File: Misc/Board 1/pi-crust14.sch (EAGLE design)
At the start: 43 parts, among them IC10 40193N, IC2 74LS595D, IC3 74LS595D, IC4 74LS595D, IC5 74LS595D, IC6 74LS595D, IC7 74LS595D, IC8 74AC11008, U1 AD9983AKSTZ_140, U2 SN54LS253_J_16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

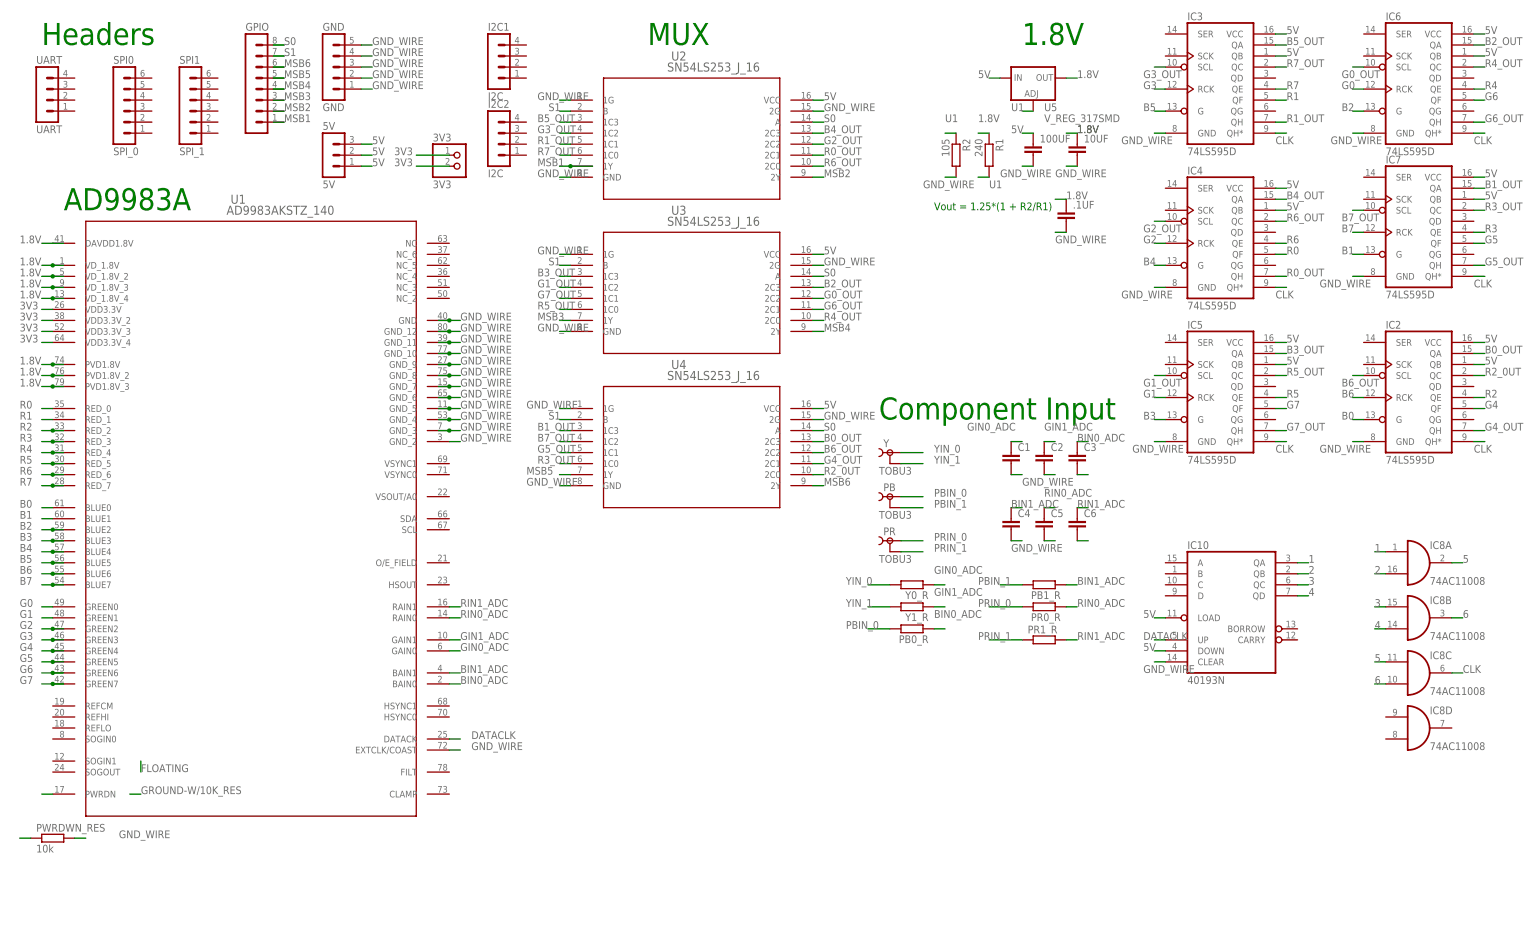
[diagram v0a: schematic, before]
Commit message: Board Update 4
Email sent to CUI for RCA Eagle File, RPI 2 female pins added to board,
ADC pins configured
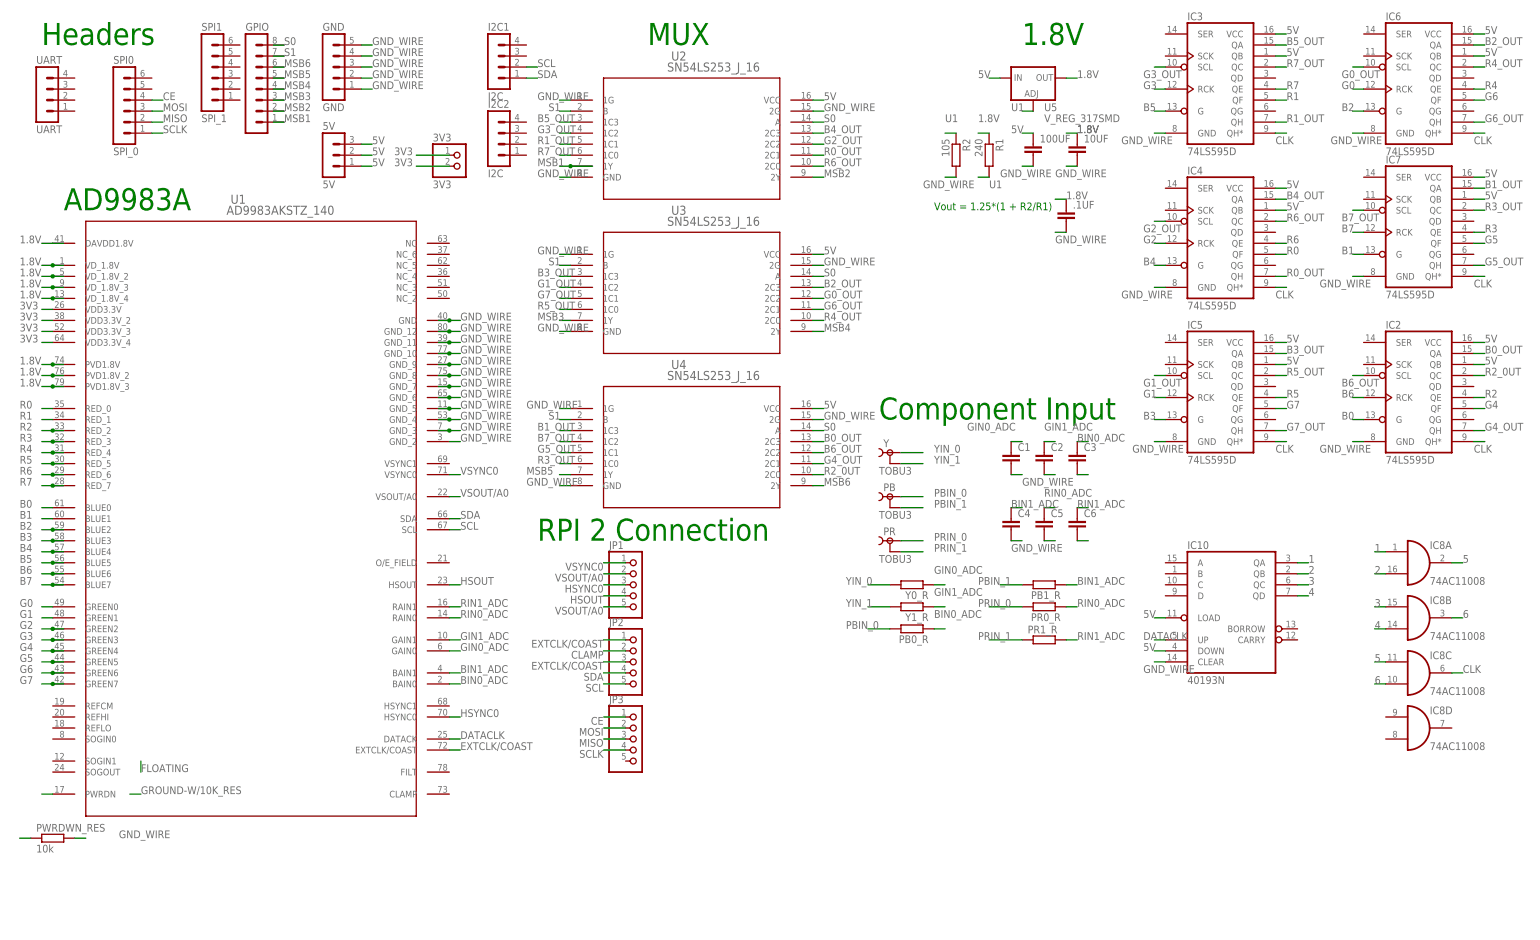
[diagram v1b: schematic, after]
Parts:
- added JP1, JP2, JP3: (no value), pinhead:PINHD-1X5
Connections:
- new net CE: JP3.1, SPI0.4
- new net CLAMP: JP2.2
- new net EXTCLK/COAST: JP2.1, JP2.3, U1.EXTCLK/COAST
- new net HSOUT: JP1.4, U1.HSOUT
- new net HSYNC0: JP1.3, U1.HSYNC0
- new net MISO: JP3.3, SPI0.2
- new net MOSI: JP3.2, SPI0.3
- new net SCL: I2C1.2, JP2.5, U1.SCL
- new net SCLK: JP3.4, SPI0.1
- new net SDA: I2C1.1, JP2.4, U1.SDA
- new net VSOUT/A0: JP1.2, JP1.5, U1.VSOUT/A0
- new net VSYNC0: JP1.1, U1.VSYNC0
- net GND_WIRE: no longer U1.EXTCLK/COAST
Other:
- note added: "RPI 2 Connection"
- moved on the sheet: SPI1
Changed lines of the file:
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@@
 <part name=".1UF" library="capacitor-wima" deviceset="C" device="2.5/5"/>
 <part name="U5" library="SparkFun-PowerIC" deviceset="V_REG_317" device="SMD"/>
+<part name="JP1" library="pinhead" deviceset="PINHD-1X5" device=""/>
+<part name="JP2" library="pinhead" deviceset="PINHD-1X5" device=""/>
+<part name="JP3" library="pinhead" deviceset="PINHD-1X5" device=""/>
 </parts>
 <sheets>
@@
 <text x="231.14" y="177.8" size="5.08" layer="91">1.8V</text>
 <text x="210.82" y="139.7" size="1.778" layer="91">Vout = 1.25*(1 + R2/R1)</text>
+<text x="119.38" y="63.5" size="5.08" layer="91">RPI 2 Connection</text>
 </plain>
 <instances>
@@
 <instance part="GND" gate="G$1" x="71.12" y="172.72"/>
 <instance part="SPI0" gate="1" x="22.86" y="165.1"/>
-<instance part="SPI1" gate="1" x="38.1" y="165.1"/>
+<instance part="SPI1" gate="1" x="43.18" y="172.72"/>
 <instance part="GPIO" gate="1" x="53.34" y="167.64"/>
 <instance part="3V3" gate="G$1" x="101.6" y="149.86"/>
@@
 <instance part=".1UF" gate="G$1" x="241.3" y="139.7"/>
 <instance part="U5" gate="G$1" x="233.68" y="170.18"/>
+<instance part="JP1" gate="A" x="142.24" y="53.34"/>
+<instance part="JP2" gate="A" x="142.24" y="35.56"/>
+<instance part="JP3" gate="A" x="142.24" y="17.78"/>
 </instances>
 <busses>
@@
 </segment>
 <segment>
-<wire x1="99.06" y1="15.24" x2="101.6" y2="15.24" width="0.3048" layer="91"/>
-<label x="104.14" y="15.24" size="1.778" layer="95"/>
-<pinref part="U1" gate="A" pin="EXTCLK/COAST"/>
-</segment>
-<segment>
 <wire x1="233.68" y1="149.86" x2="231.14" y2="149.86" width="0.8128" layer="91"/>
 <label x="226.06" y="147.32" size="1.778" layer="95"/>
@@
 <pinref part="U1" gate="A" pin="DATACK"/>
 <wire x1="99.06" y1="17.78" x2="101.6" y2="17.78" width="0.3048" layer="91"/>
-<label x="104.14" y="17.78" size="1.778" layer="95"/>
+<label x="101.6" y="17.78" size="1.778" layer="95"/>
 </segment>
 <segment>
@@
 </segment>
 </net>
+<net name="SDA" class="0">
+<segment>
+<pinref part="I2C1" gate="1" pin="1"/>
+<wire x1="116.84" y1="170.18" x2="119.38" y2="170.18" width="0.3048" layer="91"/>
+<label x="119.38" y="170.18" size="1.778" layer="95"/>
+</segment>
+<segment>
+<wire x1="134.62" y1="33.02" x2="139.7" y2="33.02" width="0.3048" layer="91"/>
+<label x="134.62" y="33.02" size="1.778" layer="95" rot="R180"/>
+<pinref part="JP2" gate="A" pin="4"/>
+</segment>
+<segment>
+<wire x1="99.06" y1="68.58" x2="101.6" y2="68.58" width="0.3048" layer="91"/>
+<label x="101.6" y="68.58" size="1.778" layer="95"/>
+<pinref part="U1" gate="A" pin="SDA"/>
+</segment>
+</net>
+<net name="SCL" class="0">
+<segment>
+<pinref part="I2C1" gate="1" pin="2"/>
+<wire x1="116.84" y1="172.72" x2="119.38" y2="172.72" width="0.3048" layer="91"/>
+<label x="119.38" y="172.72" size="1.778" layer="95"/>
+</segment>
+<segment>
+<wire x1="134.62" y1="30.48" x2="139.7" y2="30.48" width="0.3048" layer="91"/>
+<label x="134.62" y="30.48" size="1.778" layer="95" rot="R180"/>
+<pinref part="JP2" gate="A" pin="5"/>
+</segment>
+<segment>
+<wire x1="99.06" y1="66.04" x2="101.6" y2="66.04" width="0.3048" layer="91"/>
+<label x="101.6" y="66.04" size="1.778" layer="95"/>
+<pinref part="U1" gate="A" pin="SCL"/>
+</segment>
+</net>
+<net name="SCLK" class="0">
+<segment>
+<pinref part="SPI0" gate="1" pin="1"/>
+<wire x1="30.48" y1="157.48" x2="33.02" y2="157.48" width="0.3048" layer="91"/>
+<label x="33.02" y="157.48" size="1.778" layer="95"/>
+</segment>
+<segment>
+<wire x1="134.62" y1="15.24" x2="139.7" y2="15.24" width="0.3048" layer="91"/>
+<label x="134.62" y="15.24" size="1.778" layer="95" rot="R180"/>
+<pinref part="JP3" gate="A" pin="4"/>
+</segment>
+</net>
+<net name="MISO" class="0">
+<segment>
+<pinref part="SPI0" gate="1" pin="2"/>
+<wire x1="30.48" y1="160.02" x2="33.02" y2="160.02" width="0.3048" layer="91"/>
+<label x="33.02" y="160.02" size="1.778" layer="95"/>
+</segment>
+<segment>
+<wire x1="134.62" y1="17.78" x2="139.7" y2="17.78" width="0.3048" layer="91"/>
+<label x="134.62" y="17.78" size="1.778" layer="95" rot="R180"/>
+<pinref part="JP3" gate="A" pin="3"/>
+</segment>
+</net>
+<net name="MOSI" class="0">
+<segment>
+<pinref part="SPI0" gate="1" pin="3"/>
+<wire x1="30.48" y1="162.56" x2="33.02" y2="162.56" width="0.3048" layer="91"/>
+<label x="33.02" y="162.56" size="1.778" layer="95"/>
+</segment>
+<segment>
+<wire x1="134.62" y1="20.32" x2="139.7" y2="20.32" width="0.3048" layer="91"/>
+<label x="134.62" y="20.32" size="1.778" layer="95" rot="R180"/>
+<pinref part="JP3" gate="A" pin="2"/>
+</segment>
+</net>
+<net name="CE" class="0">
+<segment>
+<pinref part="SPI0" gate="1" pin="4"/>
+<wire x1="30.48" y1="165.1" x2="33.02" y2="165.1" width="0.3048" layer="91"/>
+<label x="33.02" y="165.1" size="1.778" layer="95"/>
+</segment>
+<segment>
+<wire x1="134.62" y1="22.86" x2="139.7" y2="22.86" width="0.3048" layer="91"/>
+<label x="134.62" y="22.86" size="1.778" layer="95" rot="R180"/>
+<pinref part="JP3" gate="A" pin="1"/>
+</segment>
+</net>
+<net name="VSYNC0" class="0">
+<segment>
+<pinref part="JP1" gate="A" pin="1"/>
+<wire x1="139.7" y1="58.42" x2="134.62" y2="58.42" width="0.3048" layer="91"/>
+<label x="134.62" y="58.42" size="1.778" layer="95" rot="R180"/>
+</segment>
+<segment>
+<wire x1="101.6" y1="78.74" x2="99.06" y2="78.74" width="0.3048" layer="91"/>
+<label x="101.6" y="78.74" size="1.778" layer="95"/>
+<pinref part="U1" gate="A" pin="VSYNC0"/>
+</segment>
+</net>
+<net name="HSYNC0" class="0">
+<segment>
+<pinref part="JP1" gate="A" pin="3"/>
+<wire x1="139.7" y1="53.34" x2="134.62" y2="53.34" width="0.3048" layer="91"/>
+<label x="134.62" y="53.34" size="1.778" layer="95" rot="R180"/>
+</segment>
+<segment>
+<wire x1="101.6" y1="22.86" x2="99.06" y2="22.86" width="0.3048" layer="91"/>
+<label x="101.6" y="22.86" size="1.778" layer="95"/>
+<pinref part="U1" gate="A" pin="HSYNC0"/>
+</segment>
+</net>
+<net name="HSOUT" class="0">
+<segment>
+<pinref part="JP1" gate="A" pin="4"/>
+<wire x1="139.7" y1="50.8" x2="134.62" y2="50.8" width="0.3048" layer="91"/>
+<label x="134.62" y="50.8" size="1.778" layer="95" rot="R180"/>
+</segment>
+<segment>
+<wire x1="101.6" y1="53.34" x2="99.06" y2="53.34" width="0.3048" layer="91"/>
+<label x="101.6" y="53.34" size="1.778" layer="95"/>
+<pinref part="U1" gate="A" pin="HSOUT"/>
+</segment>
+</net>
+<net name="VSOUT/A0" class="0">
+<segment>
+<pinref part="JP1" gate="A" pin="5"/>
+<wire x1="139.7" y1="48.26" x2="134.62" y2="48.26" width="0.3048" layer="91"/>
+<label x="134.62" y="48.26" size="1.778" layer="95" rot="R180"/>
+</segment>
+<segment>
+<wire x1="139.7" y1="55.88" x2="134.62" y2="55.88" width="0.3048" layer="91"/>
+<label x="134.62" y="55.88" size="1.778" layer="95" rot="R180"/>
+<pinref part="JP1" gate="A" pin="2"/>
+</segment>
+<segment>
+<wire x1="101.6" y1="73.66" x2="99.06" y2="73.66" width="0.3048" layer="91"/>
+<label x="101.6" y="73.66" size="1.778" layer="95"/>
+<pinref part="U1" gate="A" pin="VSOUT/A0"/>
+</segment>
+</net>
+<net name="EXTCLK/COAST" class="0">
+<segment>
+<pinref part="JP2" gate="A" pin="1"/>
+<wire x1="139.7" y1="40.64" x2="134.62" y2="40.64" width="0.3048" layer="91"/>
+<label x="134.62" y="40.64" size="1.778" layer="95" rot="R180"/>
+</segment>
+<segment>
+<wire x1="99.06" y1="15.24" x2="101.6" y2="15.24" width="0.3048" layer="91"/>
+<label x="101.6" y="15.24" size="1.778" layer="95"/>
+<pinref part="U1" gate="A" pin="EXTCLK/COAST"/>
+</segment>
+<segment>
+<wire x1="139.7" y1="35.56" x2="134.62" y2="35.56" width="0.3048" layer="91"/>
+<label x="134.62" y="35.56" size="1.778" layer="95" rot="R180"/>
+<pinref part="JP2" gate="A" pin="3"/>
+</segment>
+</net>
+<net name="CLAMP" class="0">
+<segment>
+<pinref part="JP2" gate="A" pin="2"/>
+<wire x1="139.7" y1="38.1" x2="134.62" y2="38.1" width="0.3048" layer="91"/>
+<label x="134.62" y="38.1" size="1.778" layer="95" rot="R180"/>
+</segment>
+</net>
